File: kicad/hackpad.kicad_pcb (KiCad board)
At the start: 2 copper layers, 185 x 40 mm, 46 parts, among them J1 Conn_01x04_MountingPin, U1 MOUDLE-SEEEDUINO-XIAO

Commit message: update kicad
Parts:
- removed G*** (x2): LOGO, LOGO
- U1: footprint Seeed Studio XIAO Series Library:XIAO-SAMD21-DIP -> Seeed Studio XIAO Series Library:XIAO-RP2040-DIP
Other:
- board text added: "__ __ __ _____/ /___ ______/ /_ ___ ____/ / / ___/ / __ `/ ___/ __ \/ _ \/ __ / (__ ) / /_/ (__ ) / / / __/ /_/ / /____/_/\__,_/____/_/ /_/\___/\__,_/"
- board text added: "__ __ ________ / /__ _____/ /____ / ___/ _ \/ / _ \/ ___/ __/ _ \ / /__/ __/ / __(__ ) /_/ __/ \___/\___/_/\___/____/\__/\___/ ____ ____ _____/ / / __ \/ __ `/ __ / / /_/ / /_/ / /_/ / / .___/\__,_/\__,_/ /_/"

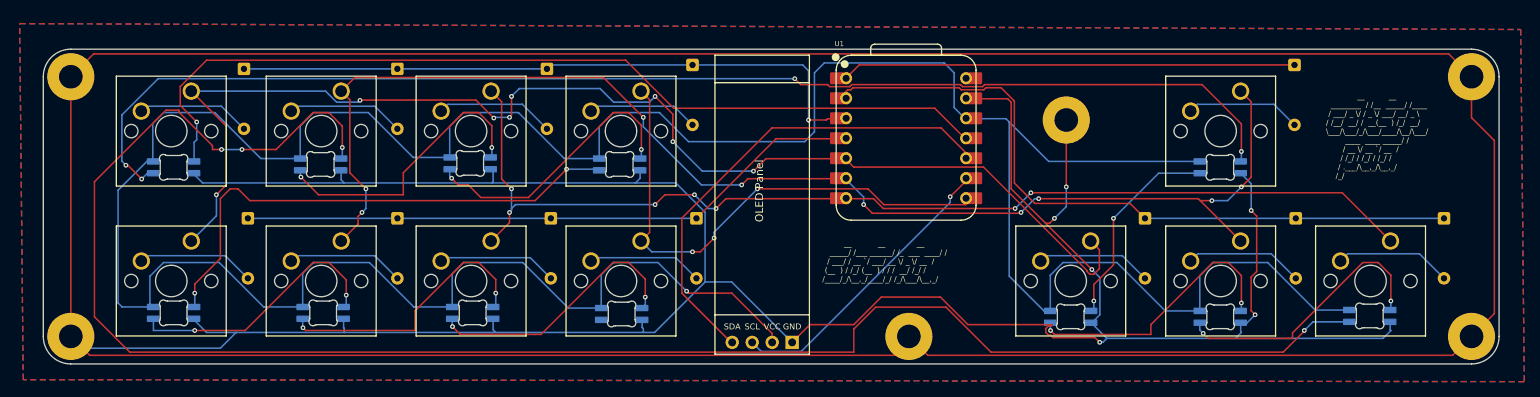
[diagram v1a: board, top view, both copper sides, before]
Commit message: update pcb to run leds on 5v
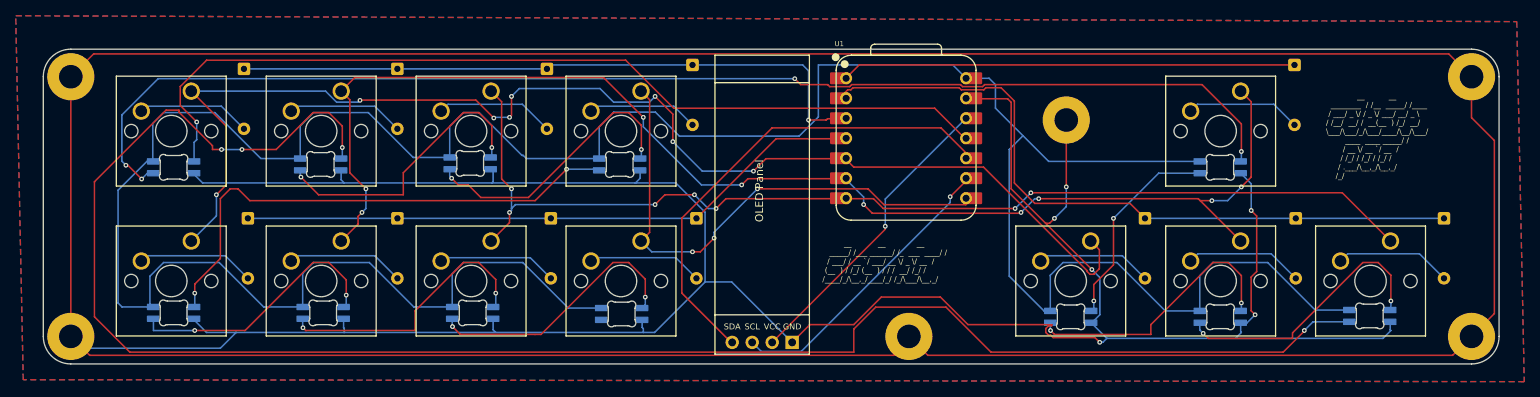
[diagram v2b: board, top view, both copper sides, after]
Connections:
- D10 pad 1: +3.3V -> +5V
- D12 pad 1: +3.3V -> +5V
- D14 pad 1: +3.3V -> +5V
- D16 pad 1: +3.3V -> +5V
- D17 pad 1: +3.3V -> +5V
- D18 pad 1: +3.3V -> +5V
- D19 pad 1: +3.3V -> +5V
- D20 pad 1: +3.3V -> +5V
- D21 pad 1: +3.3V -> +5V
- D22 pad 1: +3.3V -> +5V
- D23 pad 1: +3.3V -> +5V
- D24 pad 1: +3.3V -> +5V
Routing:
- net +5V: track 0.00 -> 358.2 mm
- net +3.3V: track 393.2 -> 38.7 mm
